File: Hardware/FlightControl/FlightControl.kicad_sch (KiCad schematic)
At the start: 5 parts

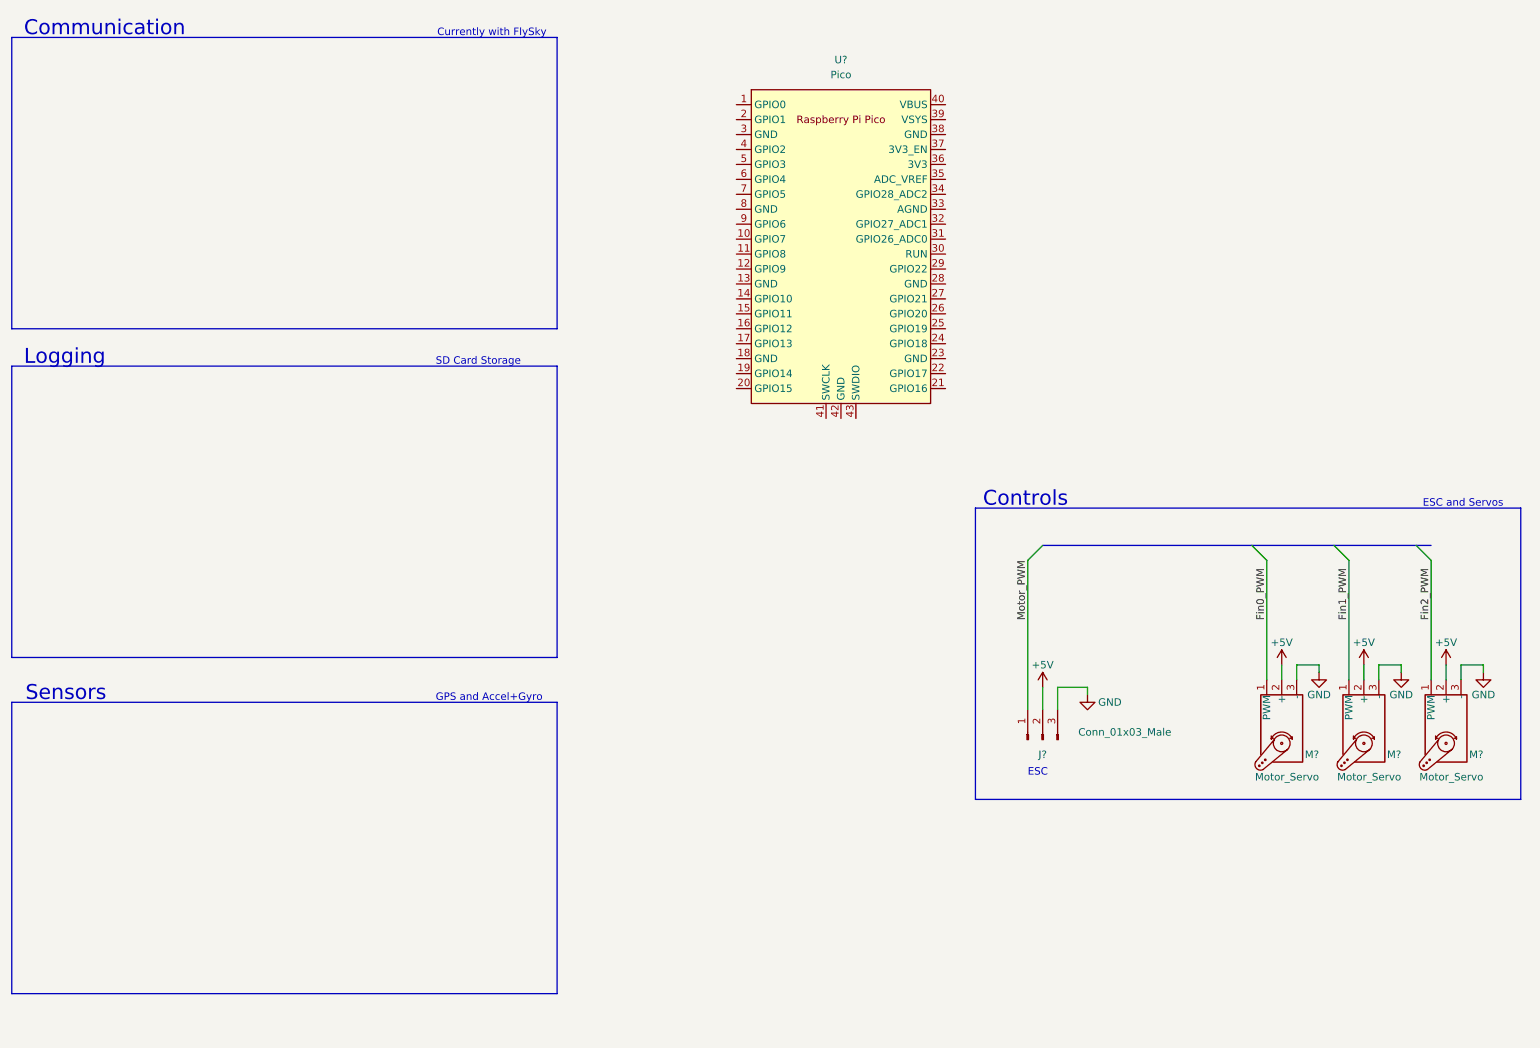
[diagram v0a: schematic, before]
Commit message: Added modules
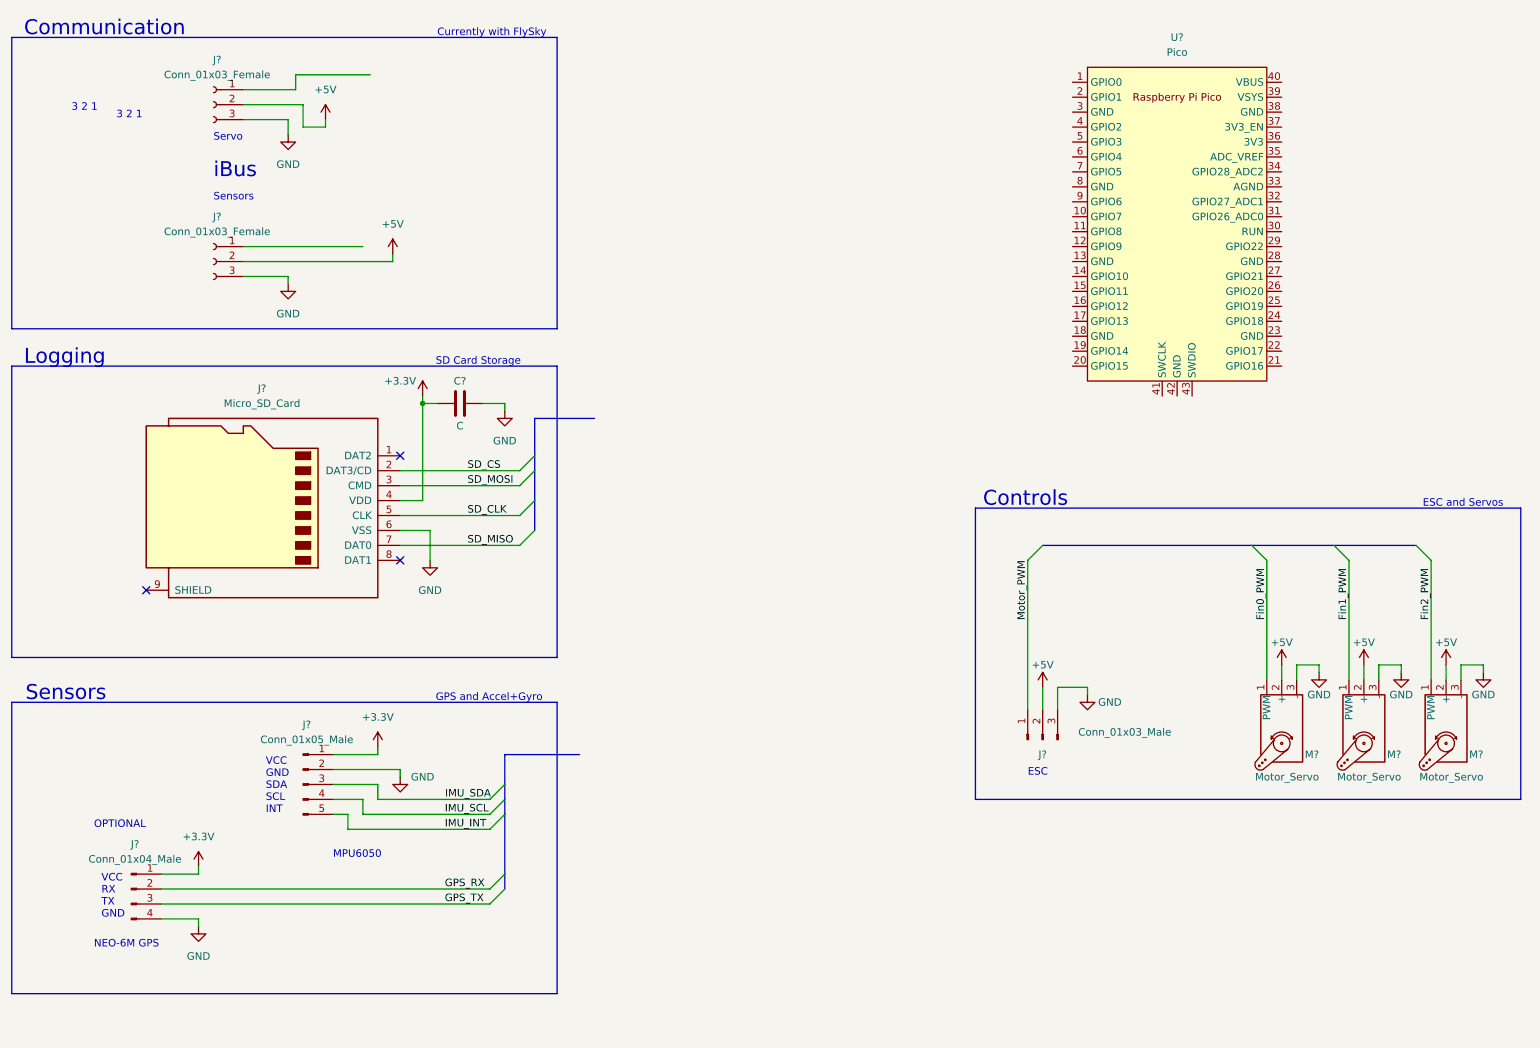
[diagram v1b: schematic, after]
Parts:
- added C?: C, symbol Device:C
- added J?: Conn_01x04_Male, symbol Connector:Conn_01x04_Male
- added J?: Micro_SD_Card, symbol Connector:Micro_SD_Card
- added J?: Conn_01x05_Male, symbol Connector:Conn_01x05_Male
- added J? (x2): Conn_01x03_Female, symbol Connector:Conn_01x03_Female
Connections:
- net +5V: now also J?.2 (Pin_2), J?.2 (Pin_2)
- net GND: now also C?.1, J?.2 (Pin_2), J?.3 (Pin_3), J?.3 (Pin_3), J?.4 (Pin_4), J?.6 (VSS)
- new net +3V3: C?.2, J?.1 (Pin_1), J?.1 (Pin_1), J?.4 (VDD)
- new net GPS_RX: J?.2 (Pin_2)
- new net GPS_TX: J?.3 (Pin_3)
- new net IMU_INT: J?.5 (Pin_5)
- new net IMU_SCL: J?.4 (Pin_4)
- new net IMU_SDA: J?.3 (Pin_3)
- new net SD_CLK: J?.5 (CLK)
- new net SD_CS: J?.2 (DAT3/CD)
- new net SD_MISO: J?.7 (DAT0)
- new net SD_MOSI: J?.3 (CMD)
- no-connect marks 0 -> 3
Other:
- note added: "3 2 1"
- note added: "MPU6050"
- note added: "NEO-6M GPS"
- note added: "OPTIONAL"
- note added: "Servo"
- note added: "VCC GND SDA SCL INT"
- note added: "VCC RX TX GND"
- note added: "iBus"
- moved on the sheet: U?

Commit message: added connections
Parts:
- added C?: C, symbol Device:C
- added J?: Conn_01x05_Male, symbol Connector:Conn_01x05_Male
- added R? (x2): 22k, symbol Device:R
- added R? (x2): 36k, symbol Device:R
- added R?: 5k, symbol Device:R
- added U?: 74LS241, symbol 74xx:74LS241
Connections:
- net +3V3: now also U?.36 (3V3), J?.1 (Pin_1)
- net +5V: now also U?.39 (VSYS), C?.2, U?.20 (VCC)
- net Fin0_PWM: now also U?.9 (O0b)
- net Fin1_PWM: now also U?.7 (O1b)
- net Fin2_PWM: now also U?.5 (O2b)
- net GND: now also U?.13 (GND), U?.18 (GND), U?.23 (GND), U?.28 (GND), U?.3 (GND), U?.33 (AGND), U?.38 (GND), U?.42 (GND), U?.8 (GND), C?.1, J?.2 (Pin_2), R?.2, R?.2, U?.10 (GND)
- net GPS_RX: now also U?.6 (GPIO4)
- net GPS_TX: now also U?.7 (GPIO5)
- net IMU_SCL: now also U?.5 (GPIO3), J?.4 (Pin_4)
- net IMU_SDA: now also U?.4 (GPIO2), J?.3 (Pin_3)
- net Motor_PWM: now also U?.3 (O3b)
- net SD_CLK: now also U?.24 (GPIO18)
- net SD_CS: now also U?.22 (GPIO17)
- net SD_MISO: now also U?.21 (GPIO16)
- net SD_MOSI: now also U?.25 (GPIO19)
- net at U?.10 (GPIO7): now also U?.13 (I1b)
- net at U?.11 (GPIO8): now also U?.15 (I2b)
- net at U?.12 (GPIO9): now also U?.17 (I3b)
- net at U?.14 (GPIO10): now also U?.1 (OEa)
- net at U?.15 (GPIO11): now also U?.19 (OEb)
- net at U?.16 (GPIO12): now also U?.2 (I0a)
- net IBUS_RX: now reaches U?.17 (GPIO13)
- net IBUS_RX: now also R?.1, R?.2
- net IBUS_Servo: now reaches U?.2 (GPIO1)
- net IBUS_Servo: now also R?.1, R?.2
- net at U?.9 (GPIO6): now also U?.11 (I0b)
- net at J?.1 (Pin_1): now also R?.1
- net at J?.1 (Pin_1): now also R?.1, R?.1
- new net IBUS_TX: R?.2, U?.18 (O0a)
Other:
- note added: ""Level Shifter""
- note added: "LSM303 Compass"
- note added: "^ MUST FIX PINOUT HERE"
- moved on the sheet: J?

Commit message: added additional details
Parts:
- added D1, D2, D3: LED, symbol Device:LED
- added R6, R7, R8: 220, symbol Device:R
- gave numbers to parts that had none: 19
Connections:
- net GND: now also U1.4 (I1a), U1.6 (I2a), U1.8 (I3a), D1.1 (K), D2.1 (K), D3.1 (K)
- net at U2.31 (GPIO26_ADC0): now also R8.1
- net at U2.32 (GPIO27_ADC1): now also R7.1
- net at U2.34 (GPIO28_ADC2): now also R6.1
- new net: D3.2 (A), R8.2
- new net: D2.2 (A), R7.2
- new net: D1.2 (A), R6.2
- no-connect marks 3 -> 10
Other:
- note added: "<- MUST FIX PINOUT HERE"
- note added: "MISSING POSSIBLE BAROMETER"
- note added: "MUST RESEARCH THE SENSORS BETTER!!"
- note added: "Simple Status UI"
- note removed: "^ MUST FIX PINOUT HERE"
- moved on the sheet: J6
